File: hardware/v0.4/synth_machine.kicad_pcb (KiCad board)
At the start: 2 copper layers, 160 x 74 mm, 120 parts, among them J1 USB-C (MIDI + 5V power), J10 Pot VOL (10k lin, panel) JST-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, J15 STEMMA QT (I2C1), J16 Power switch (panel SPST) JST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, J17 Battery 1S LiPo (JST-PH, 1 = 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, J5 Speaker L (JST-PH), J6 Speaker R (JST-PH), J7 Headphones 3.5mm (CUI SJ1-351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, J8 Expansion, J9 Display (SPI1), K1 KEY C4 (direct D10) JST-XH, K10 A4 [c2 r2] JST-XH, K11 A#4 [c1 r1] JST-XH, K12 B4 [c1 r2] JST-XH, K13 C5 [c0 r2] JST-XH, K14 BTN1 [c0 r0] JST-XH, K15 BTN2 [c0 r1] JST-XH, K16 BTN3 [c1 r0] JST-XH, K17 BTN4 [c2 r0] JST-XH, K18 BTN5 [c3 r0] JST-XH, K19 BTN6 [c4 r0] JST-XH, K2 C#4 [c5 r0] JST-XH, K3 D4 [c5 r1] JST-XH, K4 D#4 [c4 r1] JST-XH, K5 E4 [c5 r2] JST-XH, K6 F4 [c4 r2] JST-XH, K7 F#4 [c3 r1] JST-XH, K8 G4 [c3 r2] JST-XH, K9 G#4 [c2 r1] JST-XH, Q1 2N7002, Q2 2N7002, U1 Daisy Seed / Seed3, U2 TPA6138A2PWR, U3 MAX98306ETD+T, U4 USBLC6-2SC6, U5 BQ24074RGTR, U6 TPS61023DRLR

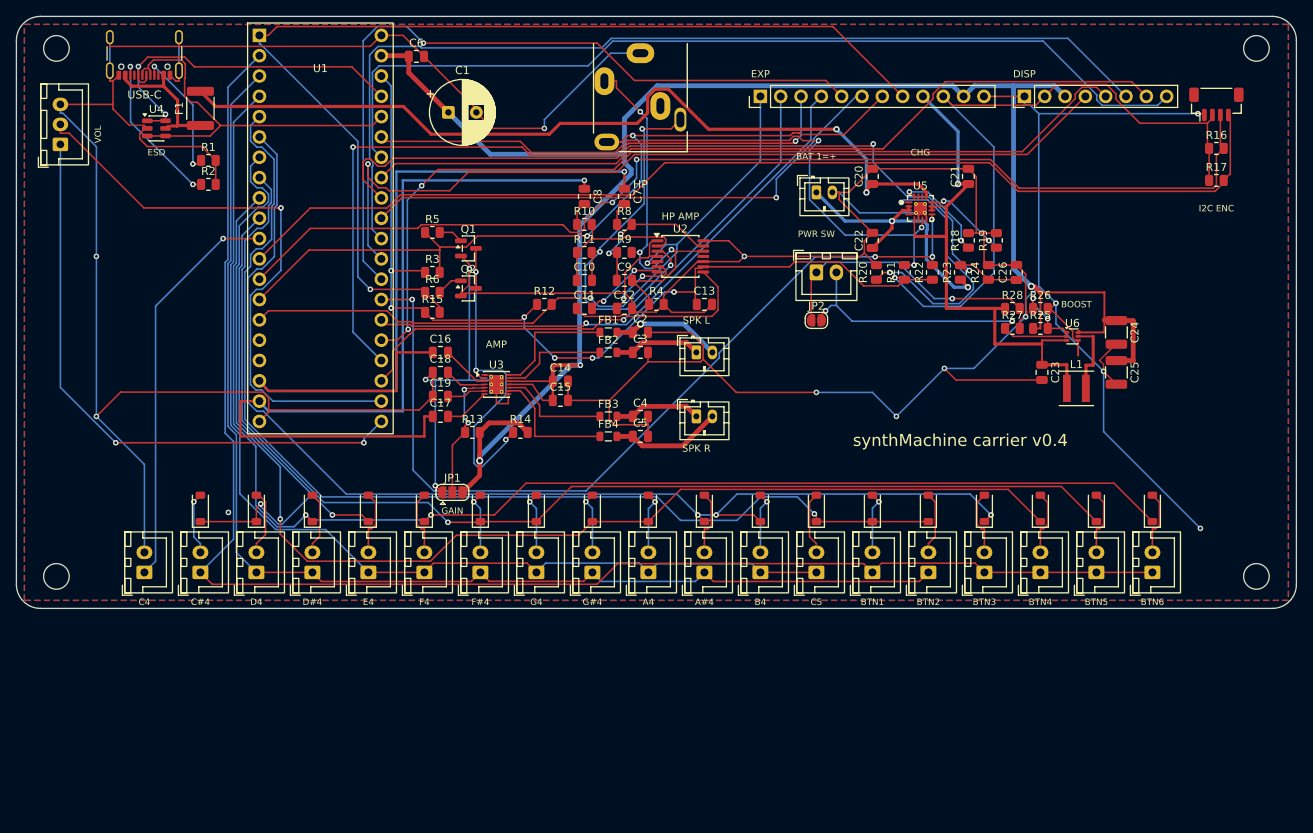
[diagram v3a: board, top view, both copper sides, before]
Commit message: Carrier v0.4: power-switch header on the left edge, jumpers given room
- J16 (panel power switch) moves to the left edge at mid-height, with JP2
  (always-on bridge) beside it instead of in the battery cluster.
- JP1 (amp gain) moves into the channel above the key diodes, clear of
  R13/R14 and the diodes, instead of squeezed between two diodes.
- Headphone-amp passive columns shifted 1 mm left so the router no longer
  needs a 0.1 mm neck past R9; route.py also widens any sub-minimum stub
  Freerouting leaves, in the pour step.
- +5V trunk from the boost to the display header pre-routed; the boost
  cluster now routes identically every run. DRC 0 unconnected, ERC clean.

Co-Authored-By: Claude Fable 5.1 <noreply@anthropic.com>
Claude-Session: https://claude.ai/code/session_019ZDGV5fm4G7LwUwRWHEiwx
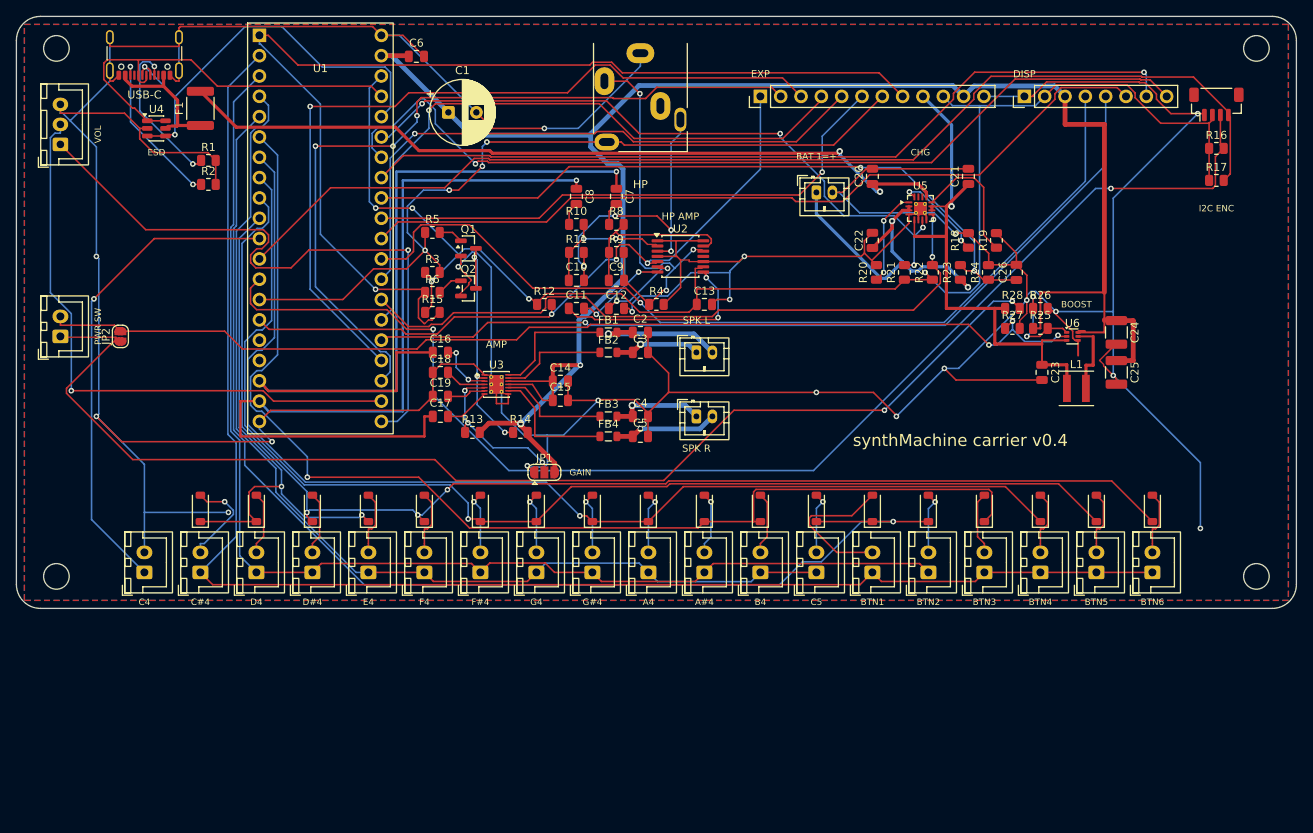
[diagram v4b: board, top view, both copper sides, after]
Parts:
- moved J16 94.8 mm to (5.50, 40.0), turned to 90 degrees
- moved JP2 87.0 mm to (13.0, 40.0), turned to 90 degrees
- moved JP1 11.8 mm to (66.0, 57.0)
- moved C10 1.00 mm to (70.0, 33.0)
- moved C11 1.00 mm to (70.0, 36.5)
- moved C12 1.00 mm to (75.0, 36.5)
- moved C7 1.00 mm to (75.0, 22.5)
- moved C8 1.00 mm to (70.0, 22.5)
- moved C9 1.00 mm to (75.0, 33.0)
- moved R10 1.00 mm to (70.0, 26.0)
- moved R11 1.00 mm to (70.0, 29.5)
- moved R8 1.00 mm to (75.0, 26.0)
- moved R9 1.00 mm to (75.0, 29.5)
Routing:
- net SW_HI: track 34.6 -> 150.9 mm, vias 1 -> 2
- net BOOST_EN: track 39.3 -> 134.6 mm, vias 2 -> 3
- net GND: track 658.9 -> 686.0 mm, vias 16 -> 20
- net EXP_A1: track 70.8 -> 97.3 mm, vias 1 -> 3
- net CHG_STAT: track 110.1 -> 85.4 mm, vias 4 -> 2
- net I2C_SDA: track 139.6 -> 161.8 mm
- net TS: track 32.8 -> 11.9 mm
- net SPI_NSS: track 122.2 -> 102.1 mm
- net EXP_A6: track 94.9 -> 76.3 mm
- net +3V3: track 204.4 -> 188.5 mm, vias 7 -> 5
- net COL0: track 135.4 -> 150.0 mm
- net EXP_A4: track 69.8 -> 82.3 mm
- net AMP_SD: track 42.8 -> 30.7 mm
- net KBTN1_D: track 7.83 -> 19.3 mm, vias 1 -> 0
- net VBAT_SENSE: track 102.4 -> 91.1 mm
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
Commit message: Carrier v0.4: JP2 4 mm further from J16 so the PWR SW label reads
Co-Authored-By: Claude Fable 5.1 <noreply@anthropic.com>
Claude-Session: https://claude.ai/code/session_019ZDGV5fm4G7LwUwRWHEiwx
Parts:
- moved JP2 4.00 mm to (17.0, 40.0)
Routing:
- net +3V3: track 188.5 -> 232.4 mm, vias 5 -> 3
- net I2C_SDA: track 161.8 -> 137.7 mm, vias 2 -> 0
- net POT_VOL: track 74.6 -> 96.7 mm
- net SPI_SCK: track 114.2 -> 97.7 mm, vias 1 -> 0
- net EXP_A2: track 100.6 -> 86.7 mm, vias 1 -> 2
- net EXP_A1: track 97.3 -> 83.8 mm, vias 3 -> 1
- net SPI_MOSI: track 108.5 -> 120.9 mm
- net USB_DM: track 55.2 -> 43.1 mm
- net KBTN1_D: track 19.3 -> 7.15 mm, vias 0 -> 1
- net SPI_NSS: track 102.1 -> 113.2 mm
- net DISP_RST: track 114.4 -> 103.8 mm, vias 1 -> 0
- net HP_L: track 50.0 -> 58.8 mm
- net VBAT_SENSE: track 91.1 -> 99.6 mm
- net EXP_A6: track 76.3 -> 83.8 mm
- net VBAT: track 42.1 -> 35.1 mm
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
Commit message: Carrier v0.4: quality pass on current paths and the boost cluster
Audit of every current-carrying net on the routed board, and fixes:
- Boost converter (SOT-563, 0.5 mm pitch rows at y 39.5/40.0/40.5): 0.3 mm
  necks off VIN/SW/VOUT/GND no longer than the pitch forces, then 0.6 mm
  into the input cap, the inductor and the output cap. Previously 0.25 mm
  for several millimetres in series with the whole battery current.
- MAX98306 PVDD pins joined right off the pads into one 0.5 mm feed; the
  four speaker lines widen to 0.4 mm as soon as they separate. Previously
  0.2 mm for the full 6 to 15 mm runs.
- +5V trunk hand-routed on both layers from the boost to the display and
  expansion headers, down between the headphone amp and the speaker
  connectors to the amp's supply, and under the jack pads on B.Cu to the
  bulk cap at the Seed's VIN. The router had been leaving a different gap
  on this net each run. Power-class (0.5 mm drill) vias throughout; the
  pre-route via helper now takes a drill size.
- FB divider resistors stood on end so the FB node is a short diagonal and
  no +5V track threads between their pads.
- Checked and documented: the TPS61023 truly disconnects in shutdown (the
  panel switch does turn everything off), 470 uF is inside its output-cap
  range, boost thermals, the Seed 3V3 budget with encoder LEDs, USB-C
  current advertisement, the ADC divider impedance, reverse-cell and
  quiescent current. Notes in the v0.4 README.
Result: DRC 0 unconnected, ERC clean.

Co-Authored-By: Claude Fable 5.1 <noreply@anthropic.com>
Claude-Session: https://claude.ai/code/session_019ZDGV5fm4G7LwUwRWHEiwx
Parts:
- moved R25 2.24 mm to (129.0, 37.0), turned to -90 degrees
- moved R26 1.12 mm to (127.0, 37.0), turned to -90 degrees
- moved R27 0.50 mm to (124.0, 39.0)
- moved R28 0.50 mm to (124.0, 36.5)
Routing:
- net +3V3: track 232.4 -> 192.9 mm
- net HP_L: track 58.8 -> 92.7 mm, vias 3 -> 4
- net SW_HI: track 153.8 -> 123.1 mm
- net POT_VOL: track 96.7 -> 67.0 mm
- net COL1: track 146.8 -> 121.8 mm, vias 1 -> 2
- net +5V: track 242.2 -> 265.4 mm, vias 3 -> 4
- net HP_R: track 32.7 -> 54.2 mm, vias 2 -> 1
- net EXP_A2: track 86.7 -> 68.4 mm, vias 2 -> 3
- net USB_PGOOD: track 82.3 -> 100.0 mm
- net COL0: track 151.4 -> 138.0 mm
- net SPI_MOSI: track 120.9 -> 108.0 mm
- net GND: track 691.0 -> 679.8 mm, vias 16 -> 18
- net EXP_A4: track 78.6 -> 67.5 mm, vias 0 -> 1
- net SPI_NSS: track 113.2 -> 102.4 mm
- net VUSB: track 106.0 -> 116.7 mm
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
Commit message: Carrier v0.4: peripheral 3.3 V rail (AP7361C-33) for encoders, display and EXP
U7, a 1 A SOT-223 LDO on +5V, makes 3V3P for the STEMMA QT connector, the
display header, the expansion header's 3V3 pin and the DNP I2C pull-ups.
The Seed's regulator now carries only the Seed, the headphone amp and the
pull-ups, so the encoder boards' NeoPixels can no longer sag it. Pinout
(1 IN, 2 GND tab, 3 OUT) checked against the AP7361C datasheet's SOT223
column; 10 uF each side placed against the footprint's stacked pins; +5V
pre-routed from the trunk to the input pin and cap, 3V3P to the output
cap. Routed: DRC 0 unconnected, ERC clean. README power section and
header tables updated.

Co-Authored-By: Claude Fable 5.1 <noreply@anthropic.com>
Claude-Session: https://claude.ai/code/session_019ZDGV5fm4G7LwUwRWHEiwx
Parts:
- added C27: 10u, C_0805_2012Metric, F.Cu at (138.0, 15.2)
- added C28: 10u, C_0805_2012Metric, F.Cu at (138.0, 25.5)
- added U7: AP7361C-33E-13, SOT-223-3_TabPin2, F.Cu at (141.0, 20.0)
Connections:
- J15 pad 2: +3V3 -> +3V3P
- J8 pad 10: +3V3 -> +3V3P
- J9 pad 2: +3V3 -> +3V3P
- R16 pad 1: +3V3 -> +3V3P
- R17 pad 1: +3V3 -> +3V3P
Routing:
- net +3V3: track 192.9 -> 125.7 mm, vias 3 -> 5
- net +3V3P: track 0.00 -> 61.0 mm, vias 0 -> 2
- net GND: track 679.8 -> 737.2 mm, vias 18 -> 15
- net HP_L: track 92.7 -> 57.6 mm, vias 4 -> 2
- net MUTE: track 125.8 -> 159.0 mm, vias 3 -> 1
- net EXP_A2: track 68.4 -> 93.1 mm, vias 3 -> 1
- net COL2: track 158.5 -> 136.8 mm, vias 1 -> 5
- net I2C_SDA: track 137.7 -> 157.9 mm, vias 0 -> 4
- net COL0: track 138.0 -> 119.2 mm, vias 1 -> 3
- net EXP_A4: track 67.5 -> 86.4 mm
- net +3.3VA: track 86.2 -> 68.2 mm
- net SPI_MOSI: track 108.0 -> 124.4 mm, vias 1 -> 2
- net EXP_A1: track 81.8 -> 98.0 mm
- net COL1: track 121.8 -> 137.2 mm, vias 2 -> 1
- net BOOST_EN: track 145.1 -> 132.2 mm
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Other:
- board text added: "3V3P"

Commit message: Carrier v0.4: JP1 (amp gain) moved to the open area right of the speaker connectors
4 mm or more clear on every side for soldering; it was 2 mm from the key
diode row. DRC 0 unconnected, ERC clean.

Co-Authored-By: Claude Fable 5.1 <noreply@anthropic.com>
Claude-Session: https://claude.ai/code/session_019ZDGV5fm4G7LwUwRWHEiwx
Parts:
- moved JP1 31.8 mm to (95.0, 44.0), turned to 90 degrees
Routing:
- net GND: track 737.2 -> 680.7 mm, vias 15 -> 17
- net BOOST_EN: track 132.2 -> 163.0 mm
- net AMP_GAIN: track 21.1 -> 51.5 mm
- net COL0: track 119.2 -> 143.7 mm, vias 3 -> 1
- net MUTE: track 159.0 -> 135.4 mm, vias 1 -> 2
- net I2C_SDA: track 157.9 -> 139.2 mm, vias 4 -> 0
- net COL2: track 136.8 -> 153.4 mm, vias 5 -> 1
- net POT_VOL: track 79.0 -> 67.0 mm, vias 2 -> 1
- net COL1: track 137.2 -> 149.0 mm, vias 1 -> 2
- net EXP_A1: track 98.0 -> 86.5 mm
- net USB_PGOOD: track 100.1 -> 89.3 mm, vias 3 -> 2
- net SPI_MOSI: track 124.4 -> 134.7 mm, vias 2 -> 1
- net EXP_A4: track 86.4 -> 77.9 mm, vias 1 -> 2
- net VBAT: track 35.0 -> 43.4 mm
- net VUSB: track 108.8 -> 116.8 mm
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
